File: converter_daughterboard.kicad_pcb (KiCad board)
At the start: 2 copper layers, 105.4 x 65.3 mm, 47 parts, among them P1 IN+, P11 SC-, P2 IN GND, P3 OUT+, P4 OUT GND, P5 PC, P6 PR, P7 SC+, P8 IC_POW-, P9 IC_POW+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

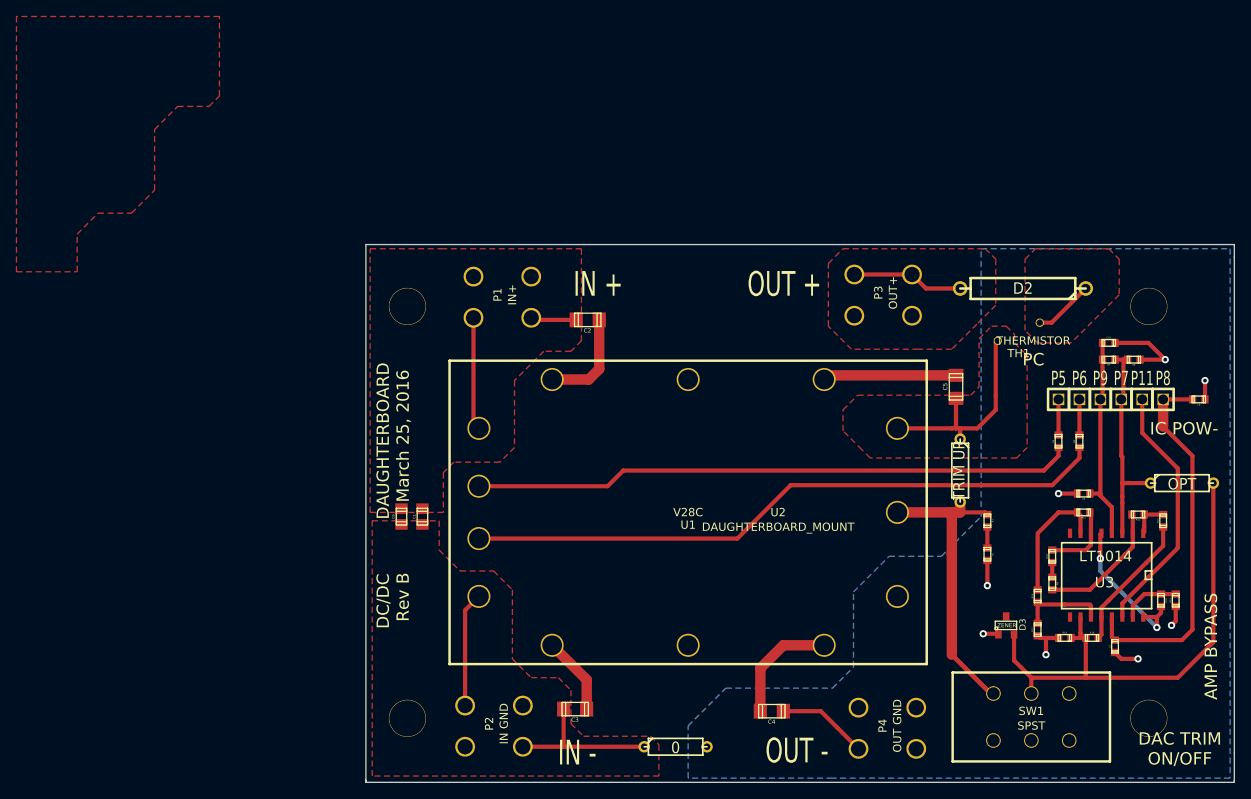
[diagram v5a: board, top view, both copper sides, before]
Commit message: revised converter daughterboard to adjust setpoint signal to account for current dropped across low side sense resistor
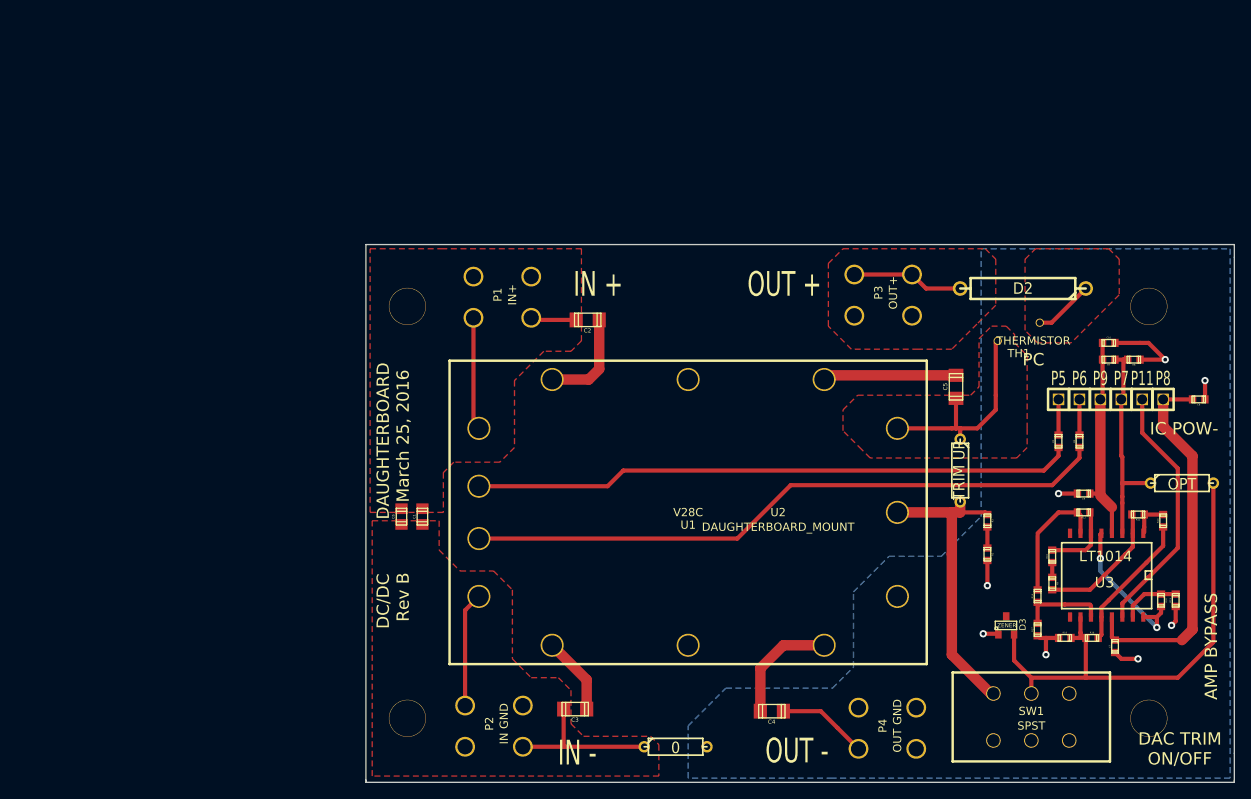
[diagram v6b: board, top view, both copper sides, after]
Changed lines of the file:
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@@
     (add_net GND)
     (add_net GNDA)
-    (add_net IC_POW-)
     (add_net N-000001)
     (add_net N-0000010)
@@
     (uvia_dia 0.508)
     (uvia_drill 0.127)
+    (add_net IC_POW-)
     (add_net N-0000019)
   )
@@
   (segment (start 162.408 164.672) (end 162.408 153.1) (width 0.512) (layer F.Cu) (net 2))
   (segment (start 162.408 153.1) (end 164.084 151.424) (width 0.512) (layer F.Cu) (net 2))
-  (segment (start 239.78616 122.682) (end 239.78616 120.65) (width 0.512) (layer F.Cu) (net 3) (status C00000))
+  (segment (start 239.78616 122.682) (end 239.78616 120.65) (width 0.512) (layer F.Cu) (net 3))
   (segment (start 239.522 127.508) (end 239.78616 127.24384) (width 0.512) (layer F.Cu) (net 3))
   (segment (start 239.78616 127.24384) (end 239.78616 122.682) (width 0.512) (layer F.Cu) (net 3))
   (segment (start 239.522 138.938) (end 238.24184 138.938) (width 0.512) (layer F.Cu) (net 3))
-  (segment (start 239.522 127.508) (end 239.522 138.938) (width 0.512) (layer F.Cu) (net 3))
+  (segment (start 239.522 127.508) (end 239.522 138.938) (width 1.27) (layer F.Cu) (net 3))
   (segment (start 239.522 138.938) (end 239.522 139.192) (width 0.512) (layer F.Cu) (net 3))
-  (segment (start 239.522 139.192) (end 240.919 140.589) (width 0.512) (layer F.Cu) (net 3))
+  (segment (start 239.522 139.192) (end 240.919 140.589) (width 1.27) (layer F.Cu) (net 3))
   (segment (start 240.919 143.764) (end 240.919 140.589) (width 0.512) (layer F.Cu) (net 3))
   (segment (start 241.3 156.72816) (end 249.41784 156.72816) (width 0.512) (layer F.Cu) (net 4))
-  (segment (start 249.41784 156.72816) (end 250.698 155.448) (width 0.512) (layer F.Cu) (net 4))
+  (segment (start 249.41784 156.72816) (end 250.698 155.448) (width 1.27) (layer F.Cu) (net 4))
   (segment (start 240.919 153.924) (end 240.919 156.34716) (width 0.512) (layer F.Cu) (net 4))
   (segment (start 240.919 156.34716) (end 241.3 156.72816) (width 0.512) (layer F.Cu) (net 4))
-  (segment (start 250.698 155.448) (end 250.698 134.366) (width 0.512) (layer F.Cu) (net 4))
+  (segment (start 250.698 155.448) (end 250.698 134.366) (width 1.27) (layer F.Cu) (net 4))
   (segment (start 247.142 127.508) (end 247.142 130.81) (width 1.27) (layer F.Cu) (net 4))
-  (segment (start 247.142 130.81) (end 250.698 134.366) (width 0.512) (layer F.Cu) (net 4))
+  (segment (start 247.142 130.81) (end 250.698 134.366) (width 1.27) (layer F.Cu) (net 4))
   (segment (start 250.70816 127.508) (end 247.142 127.508) (width 0.512) (layer F.Cu) (net 4) (status 10))
   (segment (start 235.204 152.4) (end 232.16616 152.4) (width 0.512) (layer F.Cu) (net 5))
@@
   (segment (start 225.806 141.48816) (end 225.54184 141.224) (width 0.512) (layer F.Cu) (net 13))
   (segment (start 225.54184 141.224) (end 222.504 141.224) (width 0.512) (layer F.Cu) (net 13))
-  (segment (start 226.54 163.21) (end 226.202 163.21) (width 0.512) (layer F.Cu) (net 13))
-  (segment (start 226.202 163.21) (end 221.488 158.496) (width 0.512) (layer F.Cu) (net 13))
+  (segment (start 226.54 163.21) (end 226.202 163.21) (width 1.27) (layer F.Cu) (net 13))
+  (segment (start 226.202 163.21) (end 221.488 158.496) (width 1.27) (layer F.Cu) (net 13))
   (segment (start 226.202 163.21) (end 221.488 158.496) (width 0.512) (layer F.Cu) (net 13))
   (segment (start 221.488 146.304) (end 221.488 141.224) (width 1.27) (layer F.Cu) (net 13))
@@
   (segment (start 237.236 156.464) (end 235.95584 156.464) (width 0.512) (layer F.Cu) (net 30))
   (segment (start 237.75416 156.464) (end 237.75416 161.29) (width 0.512) (layer F.Cu) (net 30))
-  (zone (net 22) (net_name N-0000030) (layer F.Cu) (hatch edge 0.508)
-    (priority 1)
-    (connect_pads (clearance 0.508))
-    (min_thickness 0.254)
-    (fill (arc_segments 16) (thermal_gap 0.508) (thermal_bridge_width 0.508))
-    (polygon
-      (pts
-        (xy 117.856 104.902) (xy 121.92 104.902) (xy 124.714 102.108) (xy 124.714 94.742) (xy 127.508 91.948)
-        (xy 131.318 91.948) (xy 132.588 90.678) (xy 132.588 81.026) (xy 107.95 81.026) (xy 107.95 112.014)
-        (xy 115.316 112.014) (xy 115.316 107.442) (xy 117.856 104.902)
-      )
-    )
-  )
   (zone (net 2) (net_name GNDA) (layer F.Cu) (hatch edge 0.508)
     (priority 1)
